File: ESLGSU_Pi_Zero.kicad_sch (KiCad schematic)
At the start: 0 parts

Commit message: Added Pi Zero W 2, continued with schematics
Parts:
- added U1: ~, ESLGSU_Parts_Lib:PI_ZERO_2_W, symbol ESLGSU_Parts_Lib:PI_ZERO_2_W
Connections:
- new net GND: U1.14 (GND), U1.20 (GND), U1.25 (GND), U1.30 (GND), U1.34 (GND), U1.39 (GND), U1.6 (GND), U1.9 (GND)
- new net PI_5V: U1.2 (5V_IN), U1.4 (5V_IN)
- new net PI_BOOT0_EPS: U1.40 (GPIO21)
- new net PI_BOOT0_MAIN: U1.37 (GPIO26)
- new net PI_BOOT0_MISC1_IO5: U1.26 (GPIO7)
- new net PI_BOOT0_MISC2_IO6: U1.15 (GPIO22)
- new net PI_I2C_SCL: U1.5 (GPIO3_SCL)
- new net PI_I2C_SDA: U1.3 (GPIO2_SDA)
- new net PI_MISO: U1.21 (GPIO9_MISO)
- new net PI_MOSI: U1.19 (GPIO10_MOSI)
- new net PI_RESET_EPS: U1.38 (GPIO20)
- new net PI_RESET_MAIN: U1.35 (GPIO19)
- new net PI_RESET_MISC1_IO3: U1.24 (GPIO8)
- new net PI_RESET_MISC2_IO4: U1.13 (GPIO27)
- new net PI_SCK: U1.23 (GPIO11_SCLK)
- new net PI_SS_EPS: U1.36 (GPIO16)
- new net PI_SS_MAIN: U1.33 (GPIO13_PWM1)
- new net PI_SS_MISC1_IO1: U1.22 (GPIO25)
- new net PI_SS_MISC2_IO2: U1.11 (GPIO17)
- new net PI_UART_RX: U1.10 (GPIO15_RX)
- new net PI_UART_TX: U1.8 (GPIO14_TX)
- no-connect marks 0 -> 10
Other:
- note added: "Pi Zero 2 W recommends a power supply capable of 2.5A Max current draw under normal conditions is around 1.5A"
- note added: "Pullups required?"

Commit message: Started work on system power section
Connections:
- net PI_BOOT0_MAIN: now also U1.12 (GPIO18); no longer U1.37 (GPIO26)
- net PI_BOOT0_MISC1_IO5: now also U1.18 (GPIO24); no longer U1.26 (GPIO7)
- net PI_BOOT0_MISC2_IO6: now also U1.13 (GPIO27); no longer U1.15 (GPIO22)
- net PI_RESET_MAIN: now also U1.11 (GPIO17); no longer U1.35 (GPIO19)
- net PI_RESET_MISC1_IO3: now also U1.16 (GPIO23); no longer U1.24 (GPIO8)
- net PI_RESET_MISC2_IO4: now also U1.37 (GPIO26); no longer U1.13 (GPIO27)
- net PI_SS_EPS: now also U1.35 (GPIO19); no longer U1.36 (GPIO16)
- net PI_SS_MAIN: now also U1.36 (GPIO16); no longer U1.33 (GPIO13_PWM1)
- net PI_SS_MISC1_IO1: now also U1.15 (GPIO22); no longer U1.22 (GPIO25)
- net PI_SS_MISC2_IO2: now also U1.22 (GPIO25); no longer U1.11 (GPIO17)
- no-connect marks 10 -> 2
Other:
- note added: "Pi Zero 2 W recommends a power supply capable of 2.5A Max current draw under high load conditions is around 1.5A"
- note removed: "Pi Zero 2 W recommends a power supply capable of 2.5A Max current draw under normal conditions is around 1.5A"

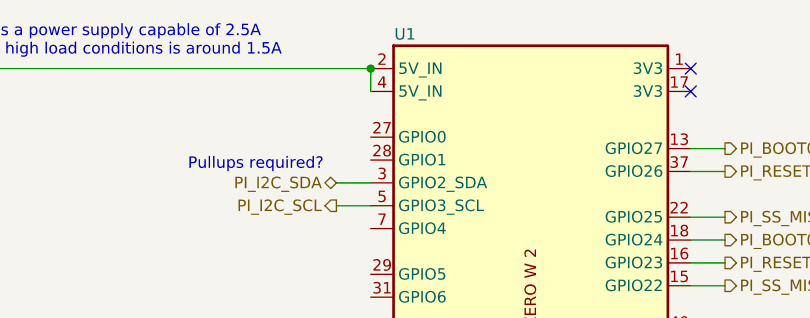
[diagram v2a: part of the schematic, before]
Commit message: Additional power regulation work
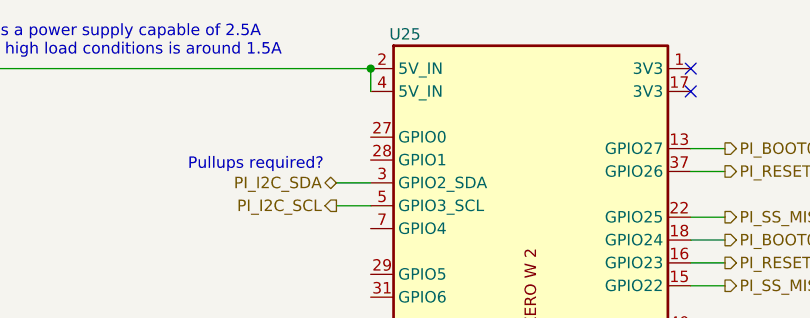
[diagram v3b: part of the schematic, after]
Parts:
- renumbered U1 to U25
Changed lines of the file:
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@@
   (symbol (lib_id "power:GND") (at 128.27 113.03 0) (unit 1)
     (in_bom yes) (on_board yes) (dnp no) (fields_autoplaced)
-    (property "Reference" "#PWR01" (at 128.27 119.38 0)
+    (property "Reference" "#PWR071" (at 128.27 119.38 0)
       (effects (font (size 1.27 1.27)) hide)
     )
@@
       (project "ESLGSU"
         (path "/b556fa32-e0cb-409c-ac85-9f2ac606be79/4575163f-435f-415b-9bb1-45133d43422d"
-          (reference "#PWR01") (unit 1)
+          (reference "#PWR071") (unit 1)
         )
       )
@@
   (symbol (lib_id "ESLGSU_Parts_Lib:PI_ZERO_2_W") (at 128.27 80.01 0) (unit 1)
     (in_bom yes) (on_board yes) (dnp no)
-    (property "Reference" "U1" (at 114.3 45.72 0)
+    (property "Reference" "U25" (at 114.3 45.72 0)
       (effects (font (size 1.27 1.27)))
     )
@@
       (project "ESLGSU"
         (path "/b556fa32-e0cb-409c-ac85-9f2ac606be79/4575163f-435f-415b-9bb1-45133d43422d"
-          (reference "U1") (unit 1)
+          (reference "U25") (unit 1)
         )
       )

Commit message: uC Interface work
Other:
- company: (none) -> Electronic Systems Laboratory
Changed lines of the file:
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@@
 (kicad_sch (version 20230121) (generator eeschema)
   (paper "A4")
+  (title_block
+    (date "2024-01-18")
+    (rev "1")
+    (company "Electronic Systems Laboratory")
+  )
   (junction (at 121.92 109.22) (diameter 0) (color 0 0 0 0)
   )

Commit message: Tried to prepare for order
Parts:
- U25: value ~ -> M20-7812045
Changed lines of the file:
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@@
       (effects (font (size 1.27 1.27)))
     )
-    (property "Value" "~" (at 129.54 81.28 0)
+    (property "Value" "M20-7812045" (at 129.54 81.28 0)
       (effects (font (size 1.27 1.27)))
     )

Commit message: Schematic work
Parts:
- U25: value M20-7812045 -> FH-00339; LCSC Part (none) -> C2685112
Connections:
- no-connect marks 2 -> 11
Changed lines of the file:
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@@
   (junction (at 124.46 109.22) (diameter 0) (color 0 0 0 0)
   )
+  (no_connect (at 110.49 74.93))
   (no_connect (at 146.05 49.53))
+  (no_connect (at 110.49 67.31))
+  (no_connect (at 110.49 82.55))
+  (no_connect (at 110.49 72.39))
   (no_connect (at 146.05 52.07))
+  (no_connect (at 110.49 80.01))
+  (no_connect (at 110.49 100.33))
+  (no_connect (at 110.49 97.79))
+  (no_connect (at 110.49 59.69))
+  (no_connect (at 110.49 57.15))
   (wire (pts (xy 149.86 60.96) (xy 146.05 60.96))
     (stroke (width 0) (type default))
@@
       (effects (font (size 1.27 1.27)))
     )
-    (property "Value" "M20-7812045" (at 129.54 81.28 0)
+    (property "Value" "FH-00339" (at 129.54 81.28 0)
       (effects (font (size 1.27 1.27)))
     )
@@
       (effects (font (size 1.27 1.27)) hide)
     )
+    (property "LCSC Part" "C2685112" (at 128.27 80.01 0)
+      (effects (font (size 1.27 1.27)) hide)
+    )

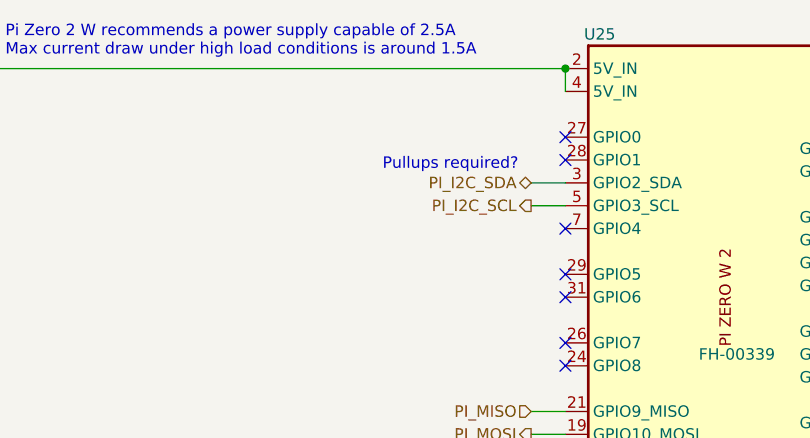
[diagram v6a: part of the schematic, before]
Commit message: Final schematic work, added battery charger, linked everything up
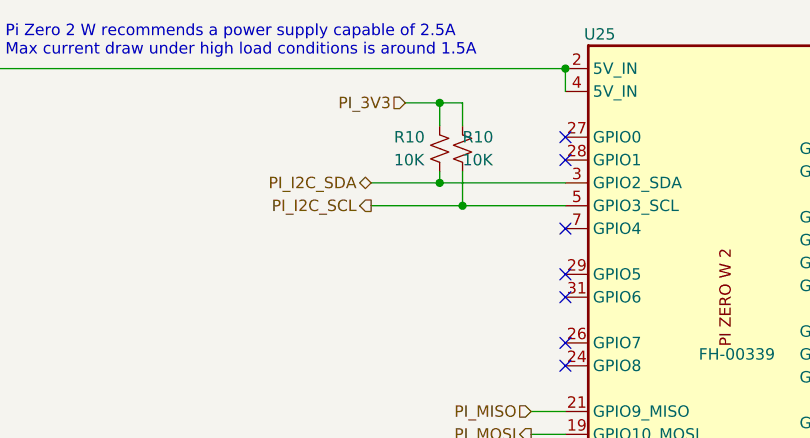
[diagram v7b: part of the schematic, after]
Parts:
- added R10 (x2): 10K, Resistor_SMD:R_0402_1005Metric, symbol Device:R_Small_US
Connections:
- net PI_I2C_SCL: now also R10.2
- net PI_I2C_SDA: now also R10.2
- new net PI_3V3: R10.1, R10.1
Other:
- note removed: "Pullups required?"
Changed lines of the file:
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@@
   (junction (at 129.54 109.22) (diameter 0) (color 0 0 0 0)
   )
+  (junction (at 96.52 53.34) (diameter 0) (color 0 0 0 0)
+  )
+  (junction (at 96.52 62.23) (diameter 0) (color 0 0 0 0)
+  )
   (junction (at 132.08 109.22) (diameter 0) (color 0 0 0 0)
   )
   (junction (at 128.27 109.22) (diameter 0) (color 0 0 0 0)
   )
+  (junction (at 99.06 64.77) (diameter 0) (color 0 0 0 0)
+  )
   (junction (at 110.49 49.53) (diameter 0) (color 0 0 0 0)
   )
@@
   )
   (no_connect (at 110.49 74.93))
-  (no_connect (at 146.05 49.53))
   (no_connect (at 110.49 67.31))
   (no_connect (at 110.49 82.55))
   (no_connect (at 110.49 72.39))
+  (no_connect (at 146.05 49.53))
   (no_connect (at 146.05 52.07))
   (no_connect (at 110.49 80.01))
@@
     (stroke (width 0) (type default))
   )
-  (wire (pts (xy 106.68 62.23) (xy 110.49 62.23))
+  (wire (pts (xy 88.9 62.23) (xy 96.52 62.23))
     (stroke (width 0) (type default))
   )
@@
     (stroke (width 0) (type default))
   )
+  (wire (pts (xy 99.06 55.88) (xy 99.06 53.34))
+    (stroke (width 0) (type default))
+  )
   (wire (pts (xy 106.68 87.63) (xy 110.49 87.63))
     (stroke (width 0) (type default))
   )
+  (wire (pts (xy 96.52 60.96) (xy 96.52 62.23))
+    (stroke (width 0) (type default))
+  )
   (wire (pts (xy 149.86 88.9) (xy 146.05 88.9))
     (stroke (width 0) (type default))
@@
     (stroke (width 0) (type default))
   )
-  (wire (pts (xy 106.68 64.77) (xy 110.49 64.77))
+  (wire (pts (xy 88.9 64.77) (xy 99.06 64.77))
     (stroke (width 0) (type default))
   )
@@
     (stroke (width 0) (type default))
   )
+  (wire (pts (xy 92.71 53.34) (xy 96.52 53.34))
+    (stroke (width 0) (type default))
+  )
+  (wire (pts (xy 99.06 60.96) (xy 99.06 64.77))
+    (stroke (width 0) (type default))
+  )
   (wire (pts (xy 128.27 109.22) (xy 129.54 109.22))
     (stroke (width 0) (type default))
@@
     (stroke (width 0) (type default))
   )
+  (wire (pts (xy 96.52 53.34) (xy 96.52 55.88))
+    (stroke (width 0) (type default))
+  )
   (wire (pts (xy 124.46 109.22) (xy 127 109.22))
     (stroke (width 0) (type default))
@@
     (stroke (width 0) (type default))
   )
+  (wire (pts (xy 96.52 62.23) (xy 110.49 62.23))
+    (stroke (width 0) (type default))
+  )
   (wire (pts (xy 106.68 92.71) (xy 110.49 92.71))
     (stroke (width 0) (type default))
@@
     (stroke (width 0) (type default))
   )
+  (wire (pts (xy 99.06 64.77) (xy 110.49 64.77))
+    (stroke (width 0) (type default))
+  )
   (wire (pts (xy 149.86 81.28) (xy 146.05 81.28))
+    (stroke (width 0) (type default))
+  )
+  (wire (pts (xy 99.06 53.34) (xy 96.52 53.34))
     (stroke (width 0) (type default))
   )
@@
     (effects (font (size 1.27 1.27)) (justify left bottom))
   )
-  (text "Pullups required?" (at 90.17 60.96 0)
-    (effects (font (size 1.27 1.27)) (justify left bottom))
-  )
   (hierarchical_label "PI_SCK" (shape output) (at 106.68 92.71 180) (fields_autoplaced)
     (effects (font (size 1.27 1.27)) (justify right))
@@
     (effects (font (size 1.27 1.27)) (justify left))
   )
-  (hierarchical_label "PI_I2C_SCL" (shape output) (at 106.68 64.77 180) (fields_autoplaced)
+  (hierarchical_label "PI_3V3" (shape input) (at 92.71 53.34 180) (fields_autoplaced)
+    (effects (font (size 1.27 1.27)) (justify right))
+  )
+  (hierarchical_label "PI_I2C_SCL" (shape output) (at 88.9 64.77 180) (fields_autoplaced)
     (effects (font (size 1.27 1.27)) (justify right))
   )
@@
     (effects (font (size 1.27 1.27)) (justify left))
   )
-  (hierarchical_label "PI_I2C_SDA" (shape bidirectional) (at 106.68 62.23 180) (fields_autoplaced)
+  (hierarchical_label "PI_I2C_SDA" (shape bidirectional) (at 88.9 62.23 180) (fields_autoplaced)
     (effects (font (size 1.27 1.27)) (justify right))
   )
@@
         (path "/b556fa32-e0cb-409c-ac85-9f2ac606be79/4575163f-435f-415b-9bb1-45133d43422d"
           (reference "#PWR071") (unit 1)
+        )
+      )
+    )
+  )
+  (symbol (lib_id "Device:R_Small_US") (at 99.06 58.42 0) (unit 1)
+    (in_bom yes) (on_board yes) (dnp no)
+    (property "Reference" "R10" (at 99.06 57.15 0)
+      (effects (font (size 1.27 1.27)) (justify left))
+    )
+    (property "Value" "10K" (at 99.06 59.69 0)
+      (effects (font (size 1.27 1.27)) (justify left))
+    )
+    (property "Footprint" "Resistor_SMD:R_0402_1005Metric" (at 99.06 58.42 0)
+      (effects (font (size 1.27 1.27)) hide)
+    )
+    (property "Datasheet" "~" (at 99.06 58.42 0)
+      (effects (font (size 1.27 1.27)) hide)
+    )
+    (property "LCSC Part" "C25744" (at 100.33 59.69 0)
+      (effects (font (size 1.27 1.27)) hide)
+    )
+    (pin "1")
+    (pin "2")
+    (instances
+      (project "ESLGSU"
+        (path "/b556fa32-e0cb-409c-ac85-9f2ac606be79/09a64186-e4de-4db7-b903-c6397ff9a54d"
+          (reference "R10") (unit 1)
+        )
+        (path "/b556fa32-e0cb-409c-ac85-9f2ac606be79/62656839-ead6-4c9d-b4ee-68fd3b49c6dd"
+          (reference "R106") (unit 1)
+        )
+        (path "/b556fa32-e0cb-409c-ac85-9f2ac606be79/c41d3519-67b9-43b9-97c4-d20822b3d6ca"
+          (reference "R222") (unit 1)
+        )
+        (path "/b556fa32-e0cb-409c-ac85-9f2ac606be79/4575163f-435f-415b-9bb1-45133d43422d"
+          (reference "R233") (unit 1)
         )
       )
@@
         )
       )
+    )
+  )
+  (symbol (lib_id "Device:R_Small_US") (at 96.52 58.42 0) (unit 1)
+    (in_bom yes) (on_board yes) (dnp no)
+    (property "Reference" "R10" (at 91.44 57.15 0)
+      (effects (font (size 1.27 1.27)) (justify left))
+    )
+    (property "Value" "10K" (at 91.44 59.69 0)
+      (effects (font (size 1.27 1.27)) (justify left))
+    )
+    (property "Footprint" "Resistor_SMD:R_0402_1005Metric" (at 96.52 58.42 0)
+      (effects (font (size 1.27 1.27)) hide)
+    )
+    (property "Datasheet" "~" (at 96.52 58.42 0)
+      (effects (font (size 1.27 1.27)) hide)
+    )
+    (property "LCSC Part" "C25744" (at 97.79 59.69 0)
+      (effects (font (size 1.27 1.27)) hide)
+    )
+    (pin "1")
+    (pin "2")
+    (instances
+      (project "ESLGSU"
+        (path "/b556fa32-e0cb-409c-ac85-9f2ac606be79/09a64186-e4de-4db7-b903-c6397ff9a54d"
+          (reference "R10") (unit 1)
+        )
+        (path "/b556fa32-e0cb-409c-ac85-9f2ac606be79/62656839-ead6-4c9d-b4ee-68fd3b49c6dd"
+          (reference "R105") (unit 1)
+        )
+        (path "/b556fa32-e0cb-409c-ac85-9f2ac606be79/c41d3519-67b9-43b9-97c4-d20822b3d6ca"
+          (reference "R221") (unit 1)
+        )
+        (path "/b556fa32-e0cb-409c-ac85-9f2ac606be79/4575163f-435f-415b-9bb1-45133d43422d"
+          (reference "R231") (unit 1)
+        )
+      )

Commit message: Last tweaks on schematic
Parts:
- renumbered U25 to U72
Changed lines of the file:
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@@
   (symbol (lib_id "power:GND") (at 128.27 113.03 0) (unit 1)
     (in_bom yes) (on_board yes) (dnp no) (fields_autoplaced)
-    (property "Reference" "#PWR071" (at 128.27 119.38 0)
+    (property "Reference" "#PWR0202" (at 128.27 119.38 0)
       (effects (font (size 1.27 1.27)) hide)
     )
@@
       (project "ESLGSU"
         (path "/b556fa32-e0cb-409c-ac85-9f2ac606be79/4575163f-435f-415b-9bb1-45133d43422d"
-          (reference "#PWR071") (unit 1)
+          (reference "#PWR0202") (unit 1)
         )
       )
@@
         )
         (path "/b556fa32-e0cb-409c-ac85-9f2ac606be79/4575163f-435f-415b-9bb1-45133d43422d"
-          (reference "R233") (unit 1)
+          (reference "R231") (unit 1)
         )
       )
@@
   (symbol (lib_id "ESLGSU_Parts_Lib:PI_ZERO_2_W") (at 128.27 80.01 0) (unit 1)
     (in_bom yes) (on_board yes) (dnp no)
-    (property "Reference" "U25" (at 114.3 45.72 0)
+    (property "Reference" "U72" (at 114.3 45.72 0)
       (effects (font (size 1.27 1.27)))
     )
@@
       (project "ESLGSU"
         (path "/b556fa32-e0cb-409c-ac85-9f2ac606be79/4575163f-435f-415b-9bb1-45133d43422d"
-          (reference "U25") (unit 1)
+          (reference "U72") (unit 1)
         )
       )
@@
         )
         (path "/b556fa32-e0cb-409c-ac85-9f2ac606be79/4575163f-435f-415b-9bb1-45133d43422d"
-          (reference "R231") (unit 1)
+          (reference "R230") (unit 1)
         )
       )
